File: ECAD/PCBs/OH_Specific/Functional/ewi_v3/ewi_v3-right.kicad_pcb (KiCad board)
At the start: 2 copper layers, 96.1 x 78.8 mm, 43 parts, among them J1 BL IN, J2 BL OUT, J3 SW, SW1 FIRE, SW2 MC/APU FIRE

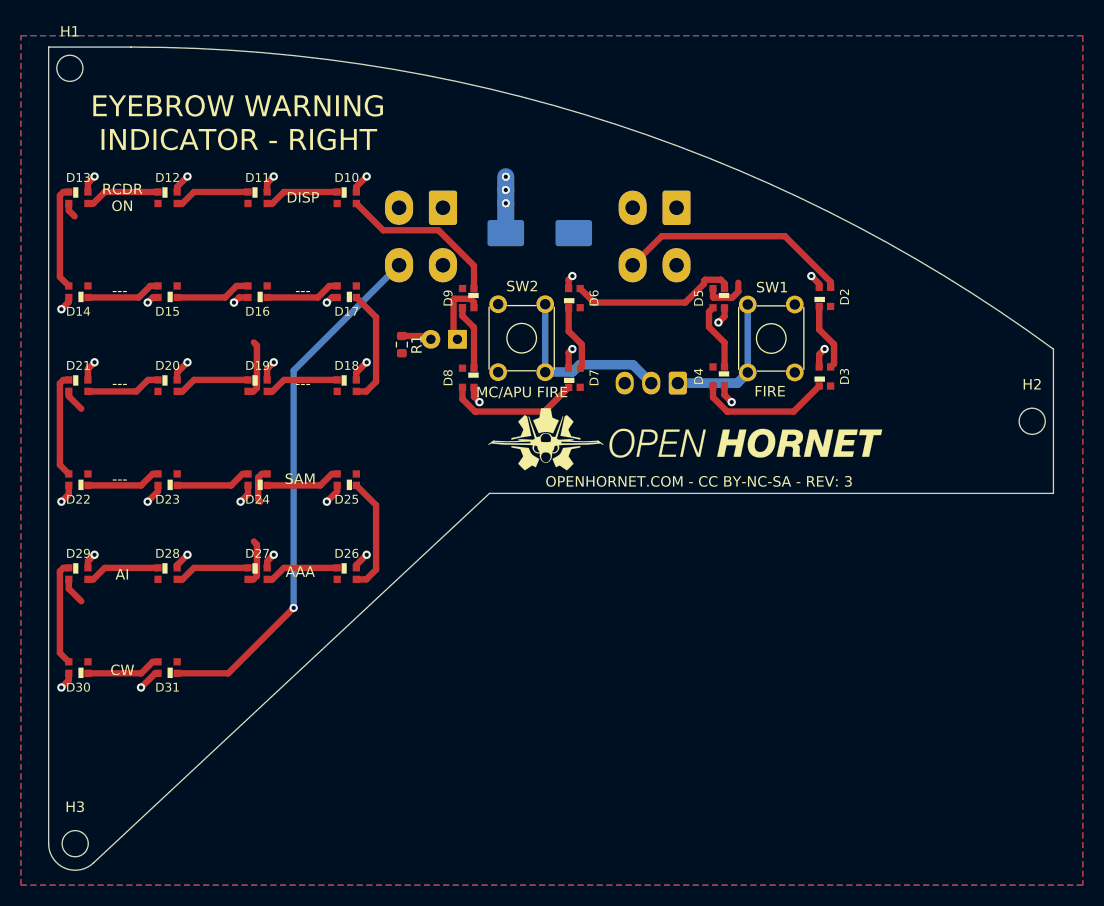
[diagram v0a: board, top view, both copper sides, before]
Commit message: EWI PCB Update
Added - 1000uF silkscreen
Added - Ready silkscreen
Changed - MC/APU Fire and Fire silkscreens down to remove collision with LEDs.
Changed - Silkscreen size and locations to match OH branding guidelines.
Changed - WS2812B-2020 LED footprint and schematic pin layout to match data sheet.
Changed - Revision from 3 to 4
Changed - Manufacturing files to match.
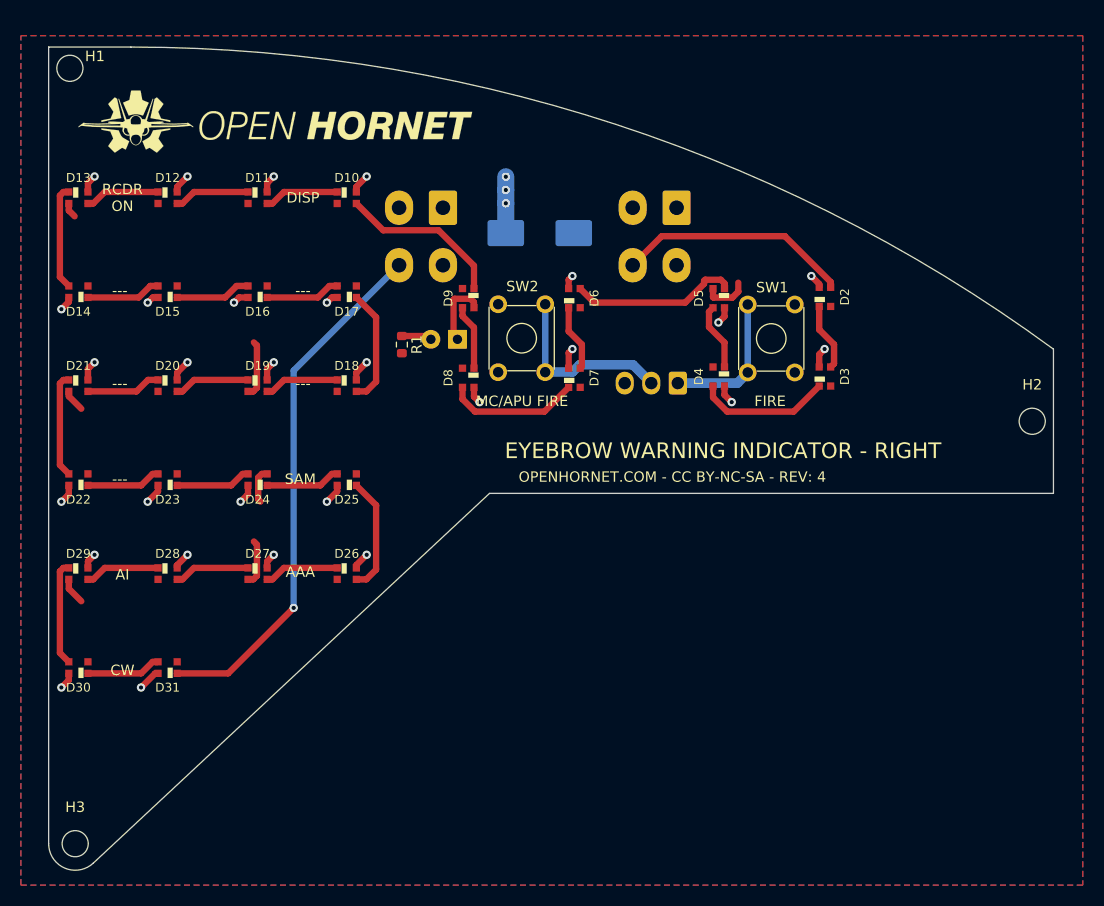
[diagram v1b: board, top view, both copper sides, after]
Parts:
- moved G*** 49.6 mm to (123.0, 64.6)
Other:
- board text added: "1000uF"
- board text added: "OPENHORNET.COM - CC BY-NC-SA - REV: 4"
- board text added: "READY"
- board text removed: "OPENHORNET.COM - CC BY-NC-SA"
- board text removed: "OPENHORNET.COM - CC BY-NC-SA - REV: 3"

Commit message: Right EWI Manufacturing File Update
Changed - LED footprint has been updated to show the current version silkscreens.
Changed - Manufacturing files to match.
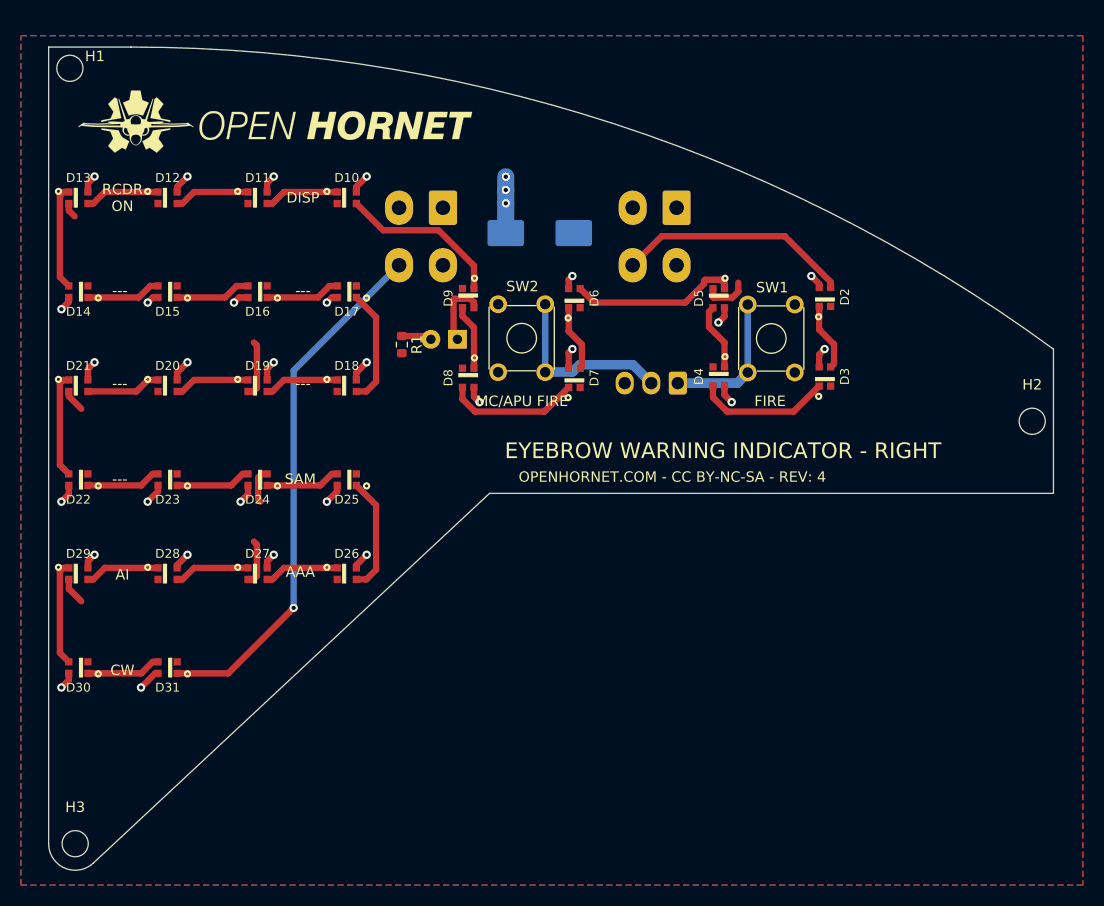
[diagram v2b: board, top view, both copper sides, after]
